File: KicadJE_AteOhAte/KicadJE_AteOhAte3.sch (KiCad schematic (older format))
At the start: 86 parts, among them J301 PJRAS2X2S01AUX, J302 Conn_01x03, U301 TL072, U302 TL072, U303 TL072

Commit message: Fused RIAA SCH
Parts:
- added F301, F302: Polyfuse, Fuse:Fuse_1206_3216Metric, symbol Device:Polyfuse
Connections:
- net GND: no longer J302.2 (Pin_2)
- net at D304.1 (K), R330.2: now also F302.1; no longer J302.1 (Pin_1)
- net at D304.2 (A): now also R327.2; no longer R327.1
- new net: F301.2, R327.1, R329.2
- new net +PSU: F301.1, J302.3 (Pin_3)
- new net -PSU: F302.2, J302.1 (Pin_1)
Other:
- moved on the sheet: C335, C336, C337, C338, C339, C340, C345, C346, D304, J302, R327, R329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

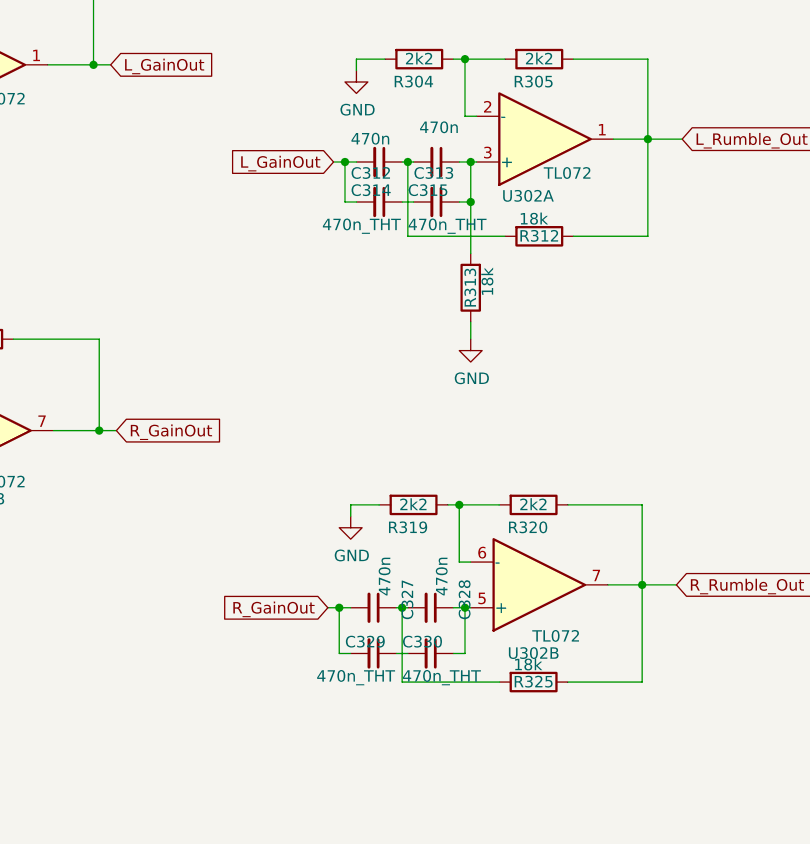
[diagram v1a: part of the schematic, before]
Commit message: SCH Error in RIAA fixed (link C313 327 area)
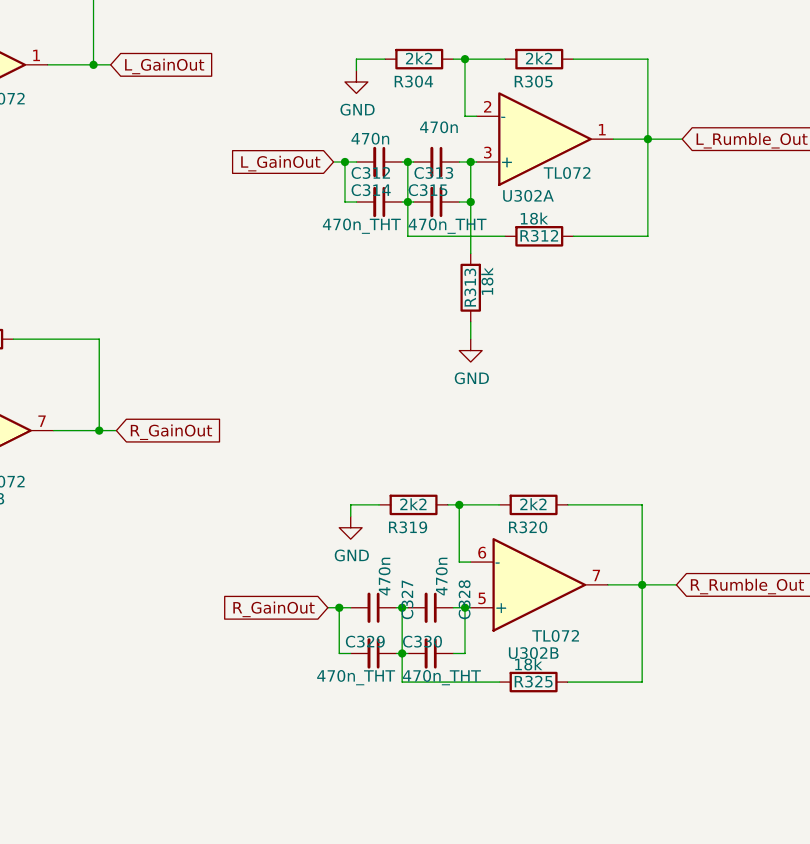
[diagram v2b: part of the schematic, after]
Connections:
- net at C312.1, C313.2, R312.2: now also C314.1, C315.2
- net at C327.1, C328.2, R325.2: now also C329.1, C330.2
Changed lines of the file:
@@
 	6675 1900 6250 1900
 Wire Wire Line
-	6250 1900 6250 1575
+	6250 1900 6250 1750
 Connection ~ 6250 1575
 Wire Wire Line
@@
 	6650 3850 6225 3850
 Wire Wire Line
-	6225 3850 6225 3525
+	6225 3850 6225 3725
 Connection ~ 6225 3525
 Wire Wire Line
@@
 $EndComp
 Wire Wire Line
-	6225 1750 6275 1750
-Wire Wire Line
 	6475 1750 6525 1750
 Wire Wire Line
@@
 Wire Wire Line
 	5950 3525 6000 3525
-Wire Wire Line
-	6200 3725 6250 3725
 Wire Wire Line
 	6500 3725 6500 3525
@@
 Wire Wire Line
 	800  6875 1500 6875
+Wire Wire Line
+	6200 3725 6225 3725
+Connection ~ 6225 3725
+Wire Wire Line
+	6225 3725 6225 3525
+Wire Wire Line
+	6225 3725 6250 3725
+Wire Wire Line
+	6225 1750 6250 1750
+Connection ~ 6250 1750
+Wire Wire Line
+	6250 1750 6250 1575
+Wire Wire Line
+	6250 1750 6275 1750
 $EndSCHEMATC
